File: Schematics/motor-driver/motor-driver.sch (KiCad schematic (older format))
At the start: 8 parts, among them J1 Conn_01x02, U1 encoder-motor, U2 encoder-motor, U3 encoder-motor, U4 encoder-motor, U5 TB6612-breakout, U6 TB6612-breakout, U7 Teensy3.2

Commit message: Make library use relative url
Change 3.3V to 5V
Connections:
- net labels added: +5V
- net labels removed: +3.3V
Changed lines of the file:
@@
 	7050 1300 7150 1300
-$Comp
-L power:+3.3V #PWR022
-U 1 1 5E2CA2E9
-P 9600 2500
-F 0 "#PWR022" H 9600 2350 50  0001 C CNN
-F 1 "+3.3V" V 9615 2628 50  0000 L CNN
-F 2 "" H 9600 2500 50  0001 C CNN
-F 3 "" H 9600 2500 50  0001 C CNN
-	1    9600 2500
-	0    1    1    0
-$EndComp
 $Comp
 L rover:TB6612-breakout U5
@@
 $EndComp
 $Comp
-L power:+3.3V #PWR06
-U 1 1 5E2E09A3
-P 2750 2700
-F 0 "#PWR06" H 2750 2550 50  0001 C CNN
-F 1 "+3.3V" V 2765 2828 50  0000 L CNN
-F 2 "" H 2750 2700 50  0001 C CNN
-F 3 "" H 2750 2700 50  0001 C CNN
-	1    2750 2700
-	0    -1   -1   0
-$EndComp
-$Comp
-L power:+3.3V #PWR01
-U 1 1 5E2E09B3
-P 2000 4750
-F 0 "#PWR01" H 2000 4600 50  0001 C CNN
-F 1 "+3.3V" V 2015 4878 50  0000 L CNN
-F 2 "" H 2000 4750 50  0001 C CNN
-F 3 "" H 2000 4750 50  0001 C CNN
-	1    2000 4750
-	0    1    1    0
-$EndComp
-$Comp
 L power:GND #PWR02
 U 1 1 5E2E09BD
@@
 	1    2000 5050
 	0    -1   -1   0
-$EndComp
-$Comp
-L power:+3.3V #PWR03
-U 1 1 5E2E09C7
-P 2050 1750
-F 0 "#PWR03" H 2050 1600 50  0001 C CNN
-F 1 "+3.3V" V 2065 1878 50  0000 L CNN
-F 2 "" H 2050 1750 50  0001 C CNN
-F 3 "" H 2050 1750 50  0001 C CNN
-	1    2050 1750
-	0    1    1    0
 $EndComp
 $Comp
@@
 STBY
 $Comp
-L power:+3.3V #PWR011
-U 1 1 5E2CAFA9
-P 5550 4200
-F 0 "#PWR011" H 5550 4050 50  0001 C CNN
-F 1 "+3.3V" V 5565 4328 50  0000 L CNN
-F 2 "" H 5550 4200 50  0001 C CNN
-F 3 "" H 5550 4200 50  0001 C CNN
-	1    5550 4200
-	0    -1   -1   0
-$EndComp
-$Comp
 L power:-BATT #PWR018
 U 1 1 5E2C92CF
@@
 	5200 5950 5600 5950
 $Comp
-L power:+3.3V #PWR016
-U 1 1 5E2CD286
-P 5600 5550
-F 0 "#PWR016" H 5600 5400 50  0001 C CNN
-F 1 "+3.3V" V 5615 5678 50  0000 L CNN
-F 2 "" H 5600 5550 50  0001 C CNN
-F 3 "" H 5600 5550 50  0001 C CNN
-	1    5600 5550
-	0    -1   -1   0
-$EndComp
-$Comp
 L power:GND #PWR017
 U 1 1 5E2CD954
@@
 	5000 1650 5600 1650
 $Comp
-L power:+3.3V #PWR014
-U 1 1 5E2CDF38
-P 5600 1750
-F 0 "#PWR014" H 5600 1600 50  0001 C CNN
-F 1 "+3.3V" V 5615 1878 50  0000 L CNN
-F 2 "" H 5600 1750 50  0001 C CNN
-F 3 "" H 5600 1750 50  0001 C CNN
-	1    5600 1750
-	0    -1   -1   0
-$EndComp
-$Comp
 L power:GND #PWR015
 U 1 1 5E2CF0C2
@@
 Wire Wire Line
 	5600 1950 4900 1950
+$Comp
+L power:+5V #PWR?
+U 1 1 5E56360A
+P 9600 4400
+F 0 "#PWR?" H 9600 4250 50  0001 C CNN
+F 1 "+5V" V 9615 4528 50  0000 L CNN
+F 2 "" H 9600 4400 50  0001 C CNN
+F 3 "" H 9600 4400 50  0001 C CNN
+	1    9600 4400
+	0    1    1    0
+$EndComp
+$Comp
+L power:+5V #PWR?
+U 1 1 5E5644C3
+P 5550 4200
+F 0 "#PWR?" H 5550 4050 50  0001 C CNN
+F 1 "+5V" V 5565 4328 50  0000 L CNN
+F 2 "" H 5550 4200 50  0001 C CNN
+F 3 "" H 5550 4200 50  0001 C CNN
+	1    5550 4200
+	0    -1   -1   0
+$EndComp
+$Comp
+L power:+5V #PWR?
+U 1 1 5E564F6F
+P 5600 5550
+F 0 "#PWR?" H 5600 5400 50  0001 C CNN
+F 1 "+5V" V 5615 5678 50  0000 L CNN
+F 2 "" H 5600 5550 50  0001 C CNN
+F 3 "" H 5600 5550 50  0001 C CNN
+	1    5600 5550
+	0    -1   -1   0
+$EndComp
+$Comp
+L power:+5V #PWR?
+U 1 1 5E5656C4
+P 5600 1750
+F 0 "#PWR?" H 5600 1600 50  0001 C CNN
+F 1 "+5V" V 5615 1878 50  0000 L CNN
+F 2 "" H 5600 1750 50  0001 C CNN
+F 3 "" H 5600 1750 50  0001 C CNN
+	1    5600 1750
+	0    -1   -1   0
+$EndComp
+$Comp
+L power:+5V #PWR?
+U 1 1 5E565BD9
+P 2750 2700
+F 0 "#PWR?" H 2750 2550 50  0001 C CNN
+F 1 "+5V" V 2765 2828 50  0000 L CNN
+F 2 "" H 2750 2700 50  0001 C CNN
+F 3 "" H 2750 2700 50  0001 C CNN
+	1    2750 2700
+	0    -1   -1   0
+$EndComp
+$Comp
+L power:+5V #PWR?
+U 1 1 5E566ACC
+P 2050 1750
+F 0 "#PWR?" H 2050 1600 50  0001 C CNN
+F 1 "+5V" V 2065 1878 50  0000 L CNN
+F 2 "" H 2050 1750 50  0001 C CNN
+F 3 "" H 2050 1750 50  0001 C CNN
+	1    2050 1750
+	0    1    1    0
+$EndComp
+$Comp
+L power:+5V #PWR?
+U 1 1 5E5671D4
+P 2000 4750
+F 0 "#PWR?" H 2000 4600 50  0001 C CNN
+F 1 "+5V" V 2015 4878 50  0000 L CNN
+F 2 "" H 2000 4750 50  0001 C CNN
+F 3 "" H 2000 4750 50  0001 C CNN
+	1    2000 4750
+	0    1    1    0
+$EndComp
 $EndSCHEMATC

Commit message: Add motor driver pcb design
Update schematics, add footprints, create pcb layout
#4
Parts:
- removed J1: Conn_01x02, symbol Connector_Generic:Conn_01x02
- added C1, C2: 0.1uF, Capacitors_THT:C_Disc_D5.0mm_W2.5mm_P5.00mm, symbol Device:CP
- added C3: 10uF, Capacitors_THT:CP_Radial_D10.0mm_P7.50mm, symbol Device:CP
- added J1: Conn_01x02_Male, Rover:AMASS_XT60-M_1x02_P7.20mm_Vertical, symbol Connector:Conn_01x02_Male
- U1, U2, U3, U4: footprint (none) -> Rover:Motor_Header_Pitch2.54mm
- U5, U6: footprint (none) -> Rover:TB661_breakout
- U7: footprint (none) -> Teensy:Teensy30_31_32_LC
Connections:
- net labels added: M1+, M1-, M2+, M2-, M3+, M3-, M4+, M4-
- wire segments 81 -> 85
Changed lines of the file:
@@
 Comment4 ""
 $EndDescr
-$Comp
-L Connector_Generic:Conn_01x02 J1
-U 1 1 5E2C1B5D
-P 6950 1100
-F 0 "J1" V 6914 912 50  0000 R CNN
-F 1 "Conn_01x02" V 6823 912 50  0000 R CNN
-F 2 "" H 6950 1100 50  0001 C CNN
-F 3 "~" H 6950 1100 50  0001 C CNN
-	1    6950 1100
-	0    -1   -1   0
-$EndComp
-$Comp
-L power:+BATT #PWR019
-U 1 1 5E2C3B2E
-P 6850 1300
-F 0 "#PWR019" H 6850 1150 50  0001 C CNN
-F 1 "+BATT" H 6865 1473 50  0000 C CNN
-F 2 "" H 6850 1300 50  0001 C CNN
-F 3 "" H 6850 1300 50  0001 C CNN
-	1    6850 1300
-	-1   0    0    1
-$EndComp
-$Comp
-L power:-BATT #PWR020
-U 1 1 5E2C61BF
-P 7150 1300
-F 0 "#PWR020" H 7150 1150 50  0001 C CNN
-F 1 "-BATT" H 7165 1473 50  0000 C CNN
-F 2 "" H 7150 1300 50  0001 C CNN
-F 3 "" H 7150 1300 50  0001 C CNN
-	1    7150 1300
-	-1   0    0    1
-$EndComp
-Wire Wire Line
-	6950 1300 6850 1300
-Wire Wire Line
-	7050 1300 7150 1300
+Wire Wire Line
+	6950 1200 6850 1200
+Wire Wire Line
+	7050 1200 7150 1200
 $Comp
 L rover:TB6612-breakout U5
@@
 F 0 "U5" H 3200 2715 50  0000 C CNN
 F 1 "TB6612-breakout" H 3200 2624 50  0000 C CNN
-F 2 "" H 3200 2500 50  0001 C CNN
+F 2 "Rover:TB661_breakout" H 3200 2500 50  0001 C CNN
 F 3 "" H 3200 2500 50  0001 C CNN
 	1    3200 2500
@@
 F 0 "U2" H 1667 4675 50  0000 C CNN
 F 1 "encoder-motor" H 1667 4584 50  0000 C CNN
-F 2 "" H 1750 4550 50  0001 C CNN
+F 2 "Rover:Motor_Header_Pitch2.54mm" H 1750 4550 50  0001 C CNN
 F 3 "" H 1750 4550 50  0001 C CNN
 	1    1750 4550
@@
 F 0 "U1" H 1717 1675 50  0000 C CNN
 F 1 "encoder-motor" H 1717 1584 50  0000 C CNN
-F 2 "" H 1800 1550 50  0001 C CNN
+F 2 "Rover:Motor_Header_Pitch2.54mm" H 1800 1550 50  0001 C CNN
 F 3 "" H 1800 1550 50  0001 C CNN
 	1    1800 1550
@@
 	4350 2500 7600 2500
 Wire Wire Line
-	7600 4400 7350 4400
-Wire Wire Line
-	7600 4300 7250 4300
+	7600 4400 7250 4400
+Wire Wire Line
+	7600 4300 7350 4300
 Wire Wire Line
 	3950 3400 7600 3400
@@
 F 0 "U7" H 8600 5087 60  0000 C CNN
 F 1 "Teensy3.2" H 8600 4981 60  0000 C CNN
-F 2 "" H 8600 2700 60  0000 C CNN
+F 2 "Teensy:Teensy30_31_32_LC" H 8600 2700 60  0001 C CNN
 F 3 "" H 8600 2700 60  0000 C CNN
 	1    8600 3450
@@
 F 0 "U6" H 6000 4215 50  0000 C CNN
 F 1 "TB6612-breakout" H 6000 4124 50  0000 C CNN
-F 2 "" H 6000 4000 50  0001 C CNN
+F 2 "Rover:TB661_breakout" H 6000 4000 50  0001 C CNN
 F 3 "" H 6000 4000 50  0001 C CNN
 	1    6000 4000
@@
 	5000 5100 9600 5100
 Wire Wire Line
-	7350 4400 7350 3600
-Wire Wire Line
-	7350 3600 4800 3600
-Wire Wire Line
-	7250 4300 7250 3700
-Wire Wire Line
-	7250 3700 4900 3700
+	7250 4400 7250 3700
+Wire Wire Line
+	7250 3700 4800 3700
+Wire Wire Line
+	7350 4300 7350 3600
+Wire Wire Line
+	7350 3600 4900 3600
 Wire Wire Line
 	5000 4400 5550 4400
@@
 F 0 "U4" H 5978 5051 50  0000 L CNN
 F 1 "encoder-motor" H 5978 4960 50  0000 L CNN
-F 2 "" H 5850 5350 50  0001 C CNN
+F 2 "Rover:Motor_Header_Pitch2.54mm" H 5850 5350 50  0001 C CNN
 F 3 "" H 5850 5350 50  0001 C CNN
 	1    5850 5350
@@
 $EndComp
 Wire Wire Line
-	4900 1950 4900 3700
-Wire Wire Line
-	4800 3600 4800 1850
+	4900 1950 4900 3600
+Wire Wire Line
+	4800 3700 4800 1850
 $Comp
 L rover:encoder-motor U3
@@
 F 0 "U3" H 5978 1251 50  0000 L CNN
 F 1 "encoder-motor" H 5978 1160 50  0000 L CNN
-F 2 "" H 5850 1550 50  0001 C CNN
+F 2 "Rover:Motor_Header_Pitch2.54mm" H 5850 1550 50  0001 C CNN
 F 3 "" H 5850 1550 50  0001 C CNN
 	1    5850 1550
@@
 	5600 1950 4900 1950
 $Comp
-L power:+5V #PWR?
+L power:+5V #PWR0101
 U 1 1 5E56360A
 P 9600 4400
-F 0 "#PWR?" H 9600 4250 50  0001 C CNN
+F 0 "#PWR0101" H 9600 4250 50  0001 C CNN
 F 1 "+5V" V 9615 4528 50  0000 L CNN
 F 2 "" H 9600 4400 50  0001 C CNN
@@
 $EndComp
 $Comp
-L power:+5V #PWR?
+L power:+5V #PWR0102
 U 1 1 5E5644C3
 P 5550 4200
-F 0 "#PWR?" H 5550 4050 50  0001 C CNN
+F 0 "#PWR0102" H 5550 4050 50  0001 C CNN
 F 1 "+5V" V 5565 4328 50  0000 L CNN
 F 2 "" H 5550 4200 50  0001 C CNN
@@
 $EndComp
 $Comp
-L power:+5V #PWR?
+L power:+5V #PWR0103
 U 1 1 5E564F6F
 P 5600 5550
-F 0 "#PWR?" H 5600 5400 50  0001 C CNN
+F 0 "#PWR0103" H 5600 5400 50  0001 C CNN
 F 1 "+5V" V 5615 5678 50  0000 L CNN
 F 2 "" H 5600 5550 50  0001 C CNN
@@
 $EndComp
 $Comp
-L power:+5V #PWR?
+L power:+5V #PWR0104
 U 1 1 5E5656C4
 P 5600 1750
-F 0 "#PWR?" H 5600 1600 50  0001 C CNN
+F 0 "#PWR0104" H 5600 1600 50  0001 C CNN
 F 1 "+5V" V 5615 1878 50  0000 L CNN
 F 2 "" H 5600 1750 50  0001 C CNN
@@
 $EndComp
 $Comp
-L power:+5V #PWR?
+L power:+5V #PWR0105
 U 1 1 5E565BD9
 P 2750 2700
-F 0 "#PWR?" H 2750 2550 50  0001 C CNN
+F 0 "#PWR0105" H 2750 2550 50  0001 C CNN
 F 1 "+5V" V 2765 2828 50  0000 L CNN
 F 2 "" H 2750 2700 50  0001 C CNN
@@
 $EndComp
 $Comp
-L power:+5V #PWR?
+L power:+5V #PWR0106
 U 1 1 5E566ACC
 P 2050 1750
-F 0 "#PWR?" H 2050 1600 50  0001 C CNN
+F 0 "#PWR0106" H 2050 1600 50  0001 C CNN
 F 1 "+5V" V 2065 1878 50  0000 L CNN
 F 2 "" H 2050 1750 50  0001 C CNN
@@
 $EndComp
 $Comp
-L power:+5V #PWR?
+L power:+5V #PWR0107
 U 1 1 5E5671D4
 P 2000 4750
-F 0 "#PWR?" H 2000 4600 50  0001 C CNN
+F 0 "#PWR0107" H 2000 4600 50  0001 C CNN
 F 1 "+5V" V 2015 4878 50  0000 L CNN
 F 2 "" H 2000 4750 50  0001 C CNN
@@
 	0    1    1    0
 $EndComp
+$Comp
+L Connector:Conn_01x02_Male J1
+U 1 1 5E2D0C6D
+P 7050 1000
+F 0 "J1" V 7112 1044 50  0000 L CNN
+F 1 "Conn_01x02_Male" V 7203 1044 50  0000 L CNN
+F 2 "Rover:AMASS_XT60-M_1x02_P7.20mm_Vertical" H 7050 1000 50  0001 C CNN
+F 3 "~" H 7050 1000 50  0001 C CNN
+	1    7050 1000
+	0    1    1    0
+$EndComp
+$Comp
+L power:+BATT #PWR019
+U 1 1 5E2C3B2E
+P 6850 1650
+F 0 "#PWR019" H 6850 1500 50  0001 C CNN
+F 1 "+BATT" H 6865 1823 50  0000 C CNN
+F 2 "" H 6850 1650 50  0001 C CNN
+F 3 "" H 6850 1650 50  0001 C CNN
+	1    6850 1650
+	-1   0    0    1
+$EndComp
+$Comp
+L power:-BATT #PWR020
+U 1 1 5E2C61BF
+P 7150 1650
+F 0 "#PWR020" H 7150 1500 50  0001 C CNN
+F 1 "-BATT" H 7165 1823 50  0000 C CNN
+F 2 "" H 7150 1650 50  0001 C CNN
+F 3 "" H 7150 1650 50  0001 C CNN
+	1    7150 1650
+	-1   0    0    1
+$EndComp
+Text Label 2200 1650 0    50   ~ 0
+M1-
+Text Label 2150 2150 0    50   ~ 0
+M1+
+Text Label 2200 5150 0    50   ~ 0
+M2+
+Text Label 2150 4650 0    50   ~ 0
+M2-
+Text Label 5150 1650 0    50   ~ 0
+M3-
+Text Label 5150 2150 0    50   ~ 0
+M3+
+Text Label 5400 5450 0    50   ~ 0
+M4-
+Text Label 5200 5950 0    50   ~ 0
+M4+
+$Comp
+L Device:CP C3
+U 1 1 5E32A80C
+P 7000 1550
+F 0 "C3" V 7255 1550 50  0000 C CNN
+F 1 "10uF" V 7164 1550 50  0000 C CNN
+F 2 "Capacitors_THT:CP_Radial_D10.0mm_P7.50mm" H 7038 1400 50  0001 C CNN
+F 3 "~" H 7000 1550 50  0001 C CNN
+	1    7000 1550
+	0    -1   -1   0
+$EndComp
+Wire Wire Line
+	6850 1200 6850 1550
+Wire Wire Line
+	6850 1550 6850 1650
+Connection ~ 6850 1550
+Wire Wire Line
+	7150 1650 7150 1550
+Wire Wire Line
+	7150 1550 7150 1200
+Connection ~ 7150 1550
+$Comp
+L power:+5V #PWR06
+U 1 1 5E33B269
+P 4500 4600
+F 0 "#PWR06" H 4500 4450 50  0001 C CNN
+F 1 "+5V" V 4515 4728 50  0000 L CNN
+F 2 "" H 4500 4600 50  0001 C CNN
+F 3 "" H 4500 4600 50  0001 C CNN
+	1    4500 4600
+	0    -1   -1   0
+$EndComp
+$Comp
+L power:GND #PWR011
+U 1 1 5E33CA86
+P 4800 4600
+F 0 "#PWR011" H 4800 4350 50  0001 C CNN
+F 1 "GND" V 4805 4472 50  0000 R CNN
+F 2 "" H 4800 4600 50  0001 C CNN
+F 3 "" H 4800 4600 50  0001 C CNN
+	1    4800 4600
+	0    -1   -1   0
+$EndComp
+$Comp
+L Device:CP C2
+U 1 1 5E338414
+P 4650 4600
+F 0 "C2" V 4905 4600 50  0000 C CNN
+F 1 "0.1uF" V 4814 4600 50  0000 C CNN
+F 2 "Capacitors_THT:C_Disc_D5.0mm_W2.5mm_P5.00mm" H 4688 4450 50  0001 C CNN
+F 3 "~" H 4650 4600 50  0001 C CNN
+	1    4650 4600
+	0    -1   -1   0
+$EndComp
+$Comp
+L power:+5V #PWR01
+U 1 1 5E34B9A8
+P 3050 3800
+F 0 "#PWR01" H 3050 3650 50  0001 C CNN
+F 1 "+5V" V 3065 3928 50  0000 L CNN
+F 2 "" H 3050 3800 50  0001 C CNN
+F 3 "" H 3050 3800 50  0001 C CNN
+	1    3050 3800
+	0    -1   -1   0
+$EndComp
+$Comp
+L power:GND #PWR03
+U 1 1 5E34B9B2
+P 3350 3800
+F 0 "#PWR03" H 3350 3550 50  0001 C CNN
+F 1 "GND" V 3355 3672 50  0000 R CNN
+F 2 "" H 3350 3800 50  0001 C CNN
+F 3 "" H 3350 3800 50  0001 C CNN
+	1    3350 3800
+	0    -1   -1   0
+$EndComp
+$Comp
+L Device:CP C1
+U 1 1 5E34B9BC
+P 3200 3800
+F 0 "C1" V 3455 3800 50  0000 C CNN
+F 1 "0.1uF" V 3364 3800 50  0000 C CNN
+F 2 "Capacitors_THT:C_Disc_D5.0mm_W2.5mm_P5.00mm" H 3238 3650 50  0001 C CNN
+F 3 "~" H 3200 3800 50  0001 C CNN
+	1    3200 3800
+	0    -1   -1   0
+$EndComp
 $EndSCHEMATC

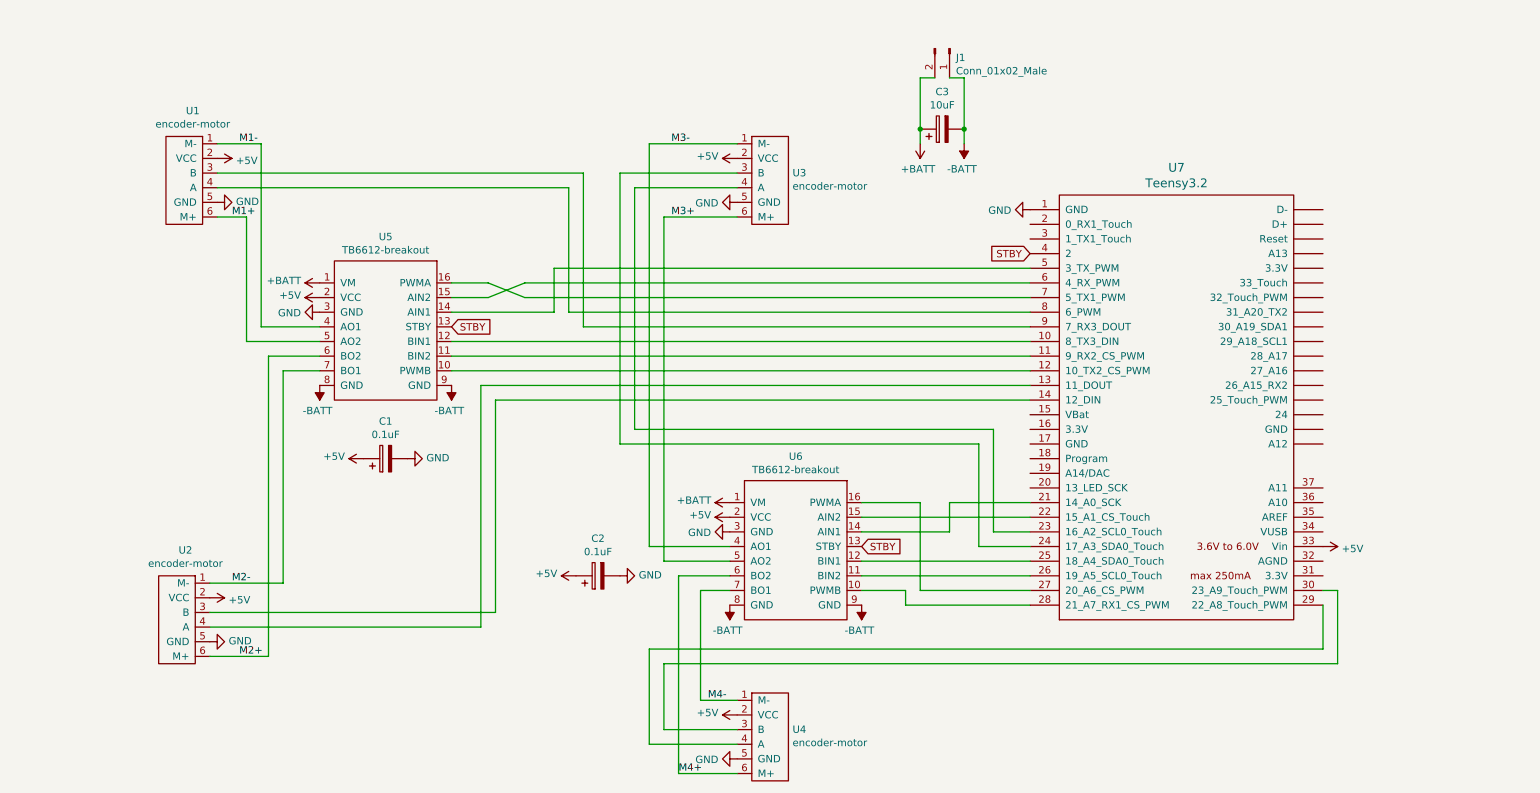
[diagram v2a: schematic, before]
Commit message: Start updating to use teensy 4.0
Need to add level shifters
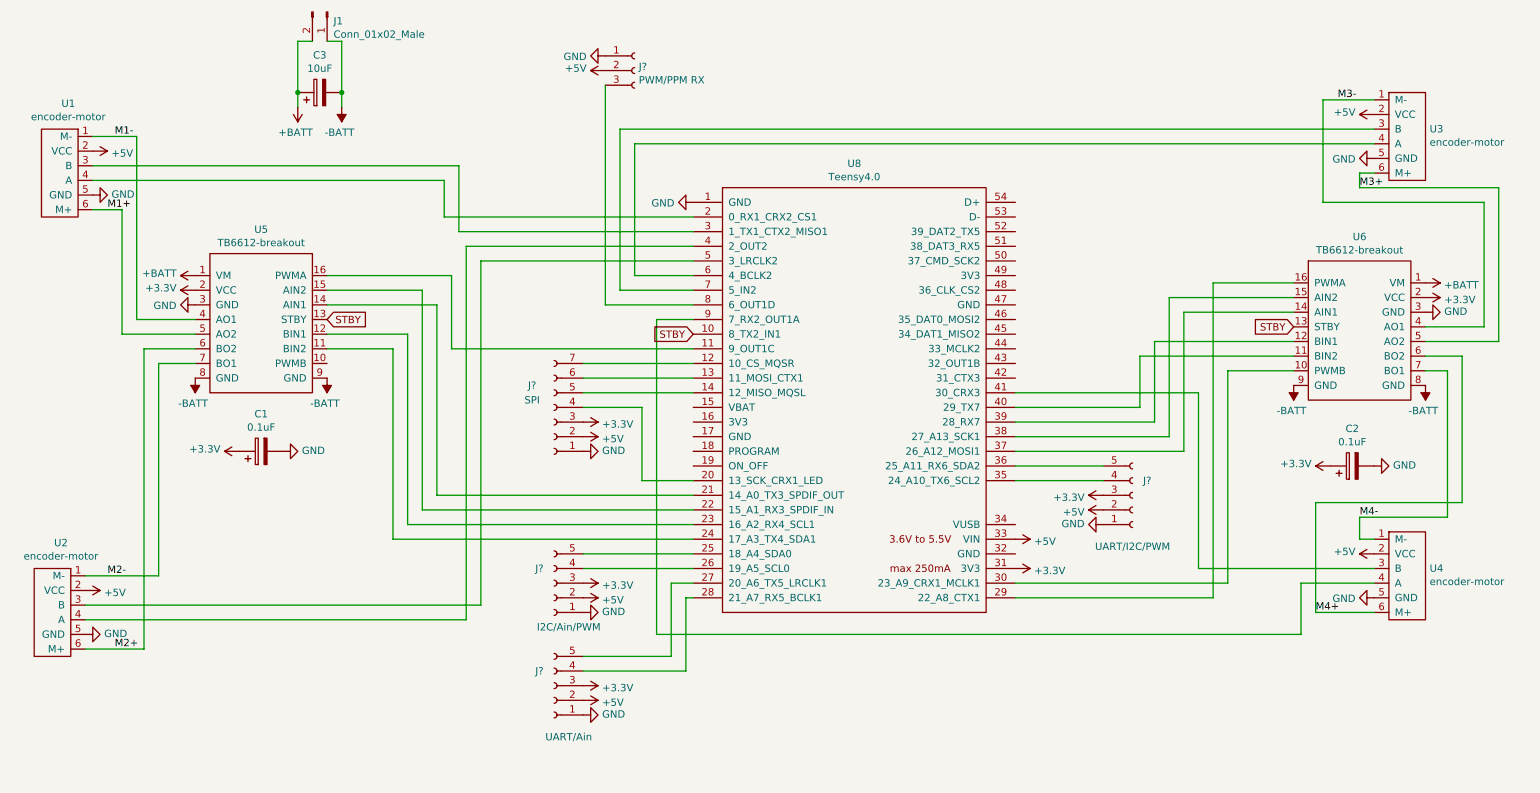
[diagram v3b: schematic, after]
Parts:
- removed U7: Teensy3.2, Teensy:Teensy30_31_32_LC, symbol Teensy:Teensy3.2
- added J?: PWM/PPM RX, symbol Connector:Conn_01x03_Female
- added J?: SPI, symbol Connector:Conn_01x07_Female
- added J?: I2C/Ain/PWM, symbol Connector:Conn_01x05_Female
- added J?: UART/Ain, symbol Connector:Conn_01x05_Female
- added J?: UART/I2C/PWM, symbol Connector:Conn_01x05_Female
- added U8: Teensy4.0, Teensy:Teensy40, symbol Teensy:Teensy4.0
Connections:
- net +5V: now also J?.2 (Pin_2), J?.2 (Pin_2), J?.2 (Pin_2), J?.2 (Pin_2), J?.2 (Pin_2), U8.33 (VIN); no longer C1.1, C2.1, U5.2 (VCC), U6.2 (VCC)
- net GND: now also J?.1 (Pin_1), J?.1 (Pin_1), J?.1 (Pin_1), J?.1 (Pin_1), J?.1 (Pin_1), U8.1 (GND)
- net STBY: now also U8.10 (8_TX2_IN1)
- net at U5.12 (BIN1): now also U8.23 (16_A2_RX4_SCL1)
- net at U5.11 (BIN2): now also U8.24 (17_A3_TX4_SDA1)
- net at U2.4 (A): now also U8.4 (2_OUT2)
- net at U2.3 (B): now also U8.5 (3_LRCLK2)
- net at U6.14 (AIN1): now also U8.37 (26_A12_MOSI1)
- net at U6.15 (AIN2): now also U8.38 (27_A13_SCK1)
- net at U3.4 (A): now also U8.6 (4_BCLK2)
- net at U3.3 (B): now also U8.7 (5_IN2)
- net at U6.12 (BIN1): now also U8.39 (28_RX7)
- net at U6.11 (BIN2): now also U8.40 (29_TX7)
- net at U6.16 (PWMA): now also U8.29 (22_A8_CTX1)
- net at U6.10 (PWMB): now also U8.30 (23_A9_CRX1_MCLK1)
- net at U4.4 (A): now also U8.9 (7_RX2_OUT1A)
- net at U4.3 (B): now also U8.41 (30_CRX3)
- net at U5.14 (AIN1): now also U8.21 (14_A0_TX3_SPDIF_OUT)
- net at U5.15 (AIN2): now also U8.22 (15_A1_RX3_SPDIF_IN)
- net at U5.16 (PWMA): now also U8.11 (9_OUT1C)
- net at U1.4 (A): now also U8.2 (0_RX1_CRX2_CS1)
- net at U1.3 (B): now also U8.3 (1_TX1_CTX2_MISO1)
- new net: J?.7 (Pin_7), U8.12 (10_CS_MQSR)
- new net: J?.6 (Pin_6), U8.13 (11_MOSI_CTX1)
- new net: J?.5 (Pin_5), U8.14 (12_MISO_MQSL)
- new net: J?.4 (Pin_4), U8.20 (13_SCK_CRX1_LED)
- new net: J?.5 (Pin_5), U8.25 (18_A4_SDA0)
- new net: J?.4 (Pin_4), U8.26 (19_A5_SCL0)
- new net: J?.5 (Pin_5), U8.27 (20_A6_TX5_LRCLK1)
- new net: J?.4 (Pin_4), U8.28 (21_A7_RX5_BCLK1)
- new net: J?.4 (Pin_4), U8.35 (24_A10_TX6_SCL2)
- new net: J?.5 (Pin_5), U8.36 (25_A11_RX6_SDA2)
- new net: J?.3 (Pin_3), U8.8 (6_OUT1D)
- new net +3V3: C1.1, C2.1, J?.3 (Pin_3), J?.3 (Pin_3), J?.3 (Pin_3), J?.3 (Pin_3), U5.2 (VCC), U6.2 (VCC), U8.31 (3V3)
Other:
- moved on the sheet: C1, C2, C3, J1, U1, U2, U3, U4, U5, U6
